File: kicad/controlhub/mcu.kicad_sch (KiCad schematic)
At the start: 0 parts

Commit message: added driver
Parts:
- added U2: ESP32-S3-DevKitC-1-N32R16V, DevKits:ESP32S3DevKitC1N32R16V, symbol DevKits:ESP32-S3-DevKitC-1-N32R16V
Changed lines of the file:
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@@
 	(generator_version "9.0")
 	(paper "A4")
+	(symbol
+		(lib_id "DevKits:ESP32-S3-DevKitC-1-N32R16V")
+		(at 127 38.1 0)
+		(unit 1)
+		(exclude_from_sim no)
+		(in_bom yes)
+		(on_board yes)
+		(dnp no)
+		(fields_autoplaced yes)
+		(property "Reference" "U2"
+			(at 140.97 30.48 0)
+			(effects
+				(font
+					(size 1.27 1.27)
+				)
+			)
+		)
+		(property "Value" "ESP32-S3-DevKitC-1-N32R16V"
+			(at 140.97 33.02 0)
+			(effects
+				(font
+					(size 1.27 1.27)
+				)
+			)
+		)
+		(property "Footprint" "DevKits:ESP32S3DevKitC1N32R16V"
+			(at 151.13 133.02 0)
+			(effects
+				(font
+					(size 1.27 1.27)
+				)
+				(justify left top)
+				(hide yes)
+			)
+		)
+		(property "Datasheet" "https://docs.espressif.com/projects/esp-dev-kits/en/latest/esp32s3/esp-dev-kits-en-master-esp32s3.pdf"
+			(at 151.13 233.02 0)
+			(effects
+				(font
+					(size 1.27 1.27)
+				)
+				(justify left top)
+				(hide yes)
+			)
+		)
+		(property "Description" "Multiprotocol Development Tools The ESP32-S3-DevKitC-1 is an entry-level development board equipped with ESP32-S3-WROOM-1, ESP32-S3-WROOM-1U, or ESP32-S3-WROOM-2, a general-purpose Wi-Fi + Bluetooth Low Energy MCU module that integrates complete Wi-Fi and Bluetooth Low Energy funct"
+			(at 127 38.1 0)
+			(effects
+				(font
+					(size 1.27 1.27)
+				)
+				(hide yes)
+			)
+		)
+		(property "Height" "5"
+			(at 151.13 433.02 0)
+			(effects
+				(font
+					(size 1.27 1.27)
+				)
+				(justify left top)
+				(hide yes)
+			)
+		)
+		(property "Manufacturer_Name" "Espressif Systems"
+			(at 151.13 533.02 0)
+			(effects
+				(font
+					(size 1.27 1.27)
+				)
+				(justify left top)
+				(hide yes)
+			)
+		)
+		(property "Manufacturer_Part_Number" "ESP32-S3-DevKitC-1-N32R16V"
+			(at 151.13 633.02 0)
+			(effects
+				(font
+					(size 1.27 1.27)
+				)
+				(justify left top)
+				(hide yes)
+			)
+		)
+		(property "Mouser Part Number" "356-32S3DKTC1N32R16V"
+			(at 151.13 733.02 0)
+			(effects
+				(font
+					(size 1.27 1.27)
+				)
+				(justify left top)
+				(hide yes)
+			)
+		)
+		(property "Mouser Price/Stock" "https://www.mouser.co.uk/ProductDetail/Espressif-Systems/ESP32-S3-DevKitC-1-N32R16V?qs=sqEgtWRSLJ3pTWIVKUeIew%3D%3D"
+			(at 151.13 833.02 0)
+			(effects
+				(font
+					(size 1.27 1.27)
+				)
+				(justify left top)
+				(hide yes)
+			)
+		)
+		(property "Arrow Part Number" ""
+			(at 151.13 933.02 0)
+			(effects
+				(font
+					(size 1.27 1.27)
+				)
+				(justify left top)
+				(hide yes)
+			)
+		)
+		(property "Arrow Price/Stock" ""
+			(at 151.13 1033.02 0)
+			(effects
+				(font
+					(size 1.27 1.27)
+				)
+				(justify left top)
+				(hide yes)
+			)
+		)
+		(pin "J332"
+		)
+		(pin "J112"
+		)
+		(pin "J116"
+		)
+		(pin "J111"
+		)
+		(pin "J113"
+		)
+		(pin "J114"
+		)
+		(pin "J115"
+		)
+		(pin "J120"
+		)
+		(pin "J317"
+		)
+		(pin "J124"
+		)
+		(pin "J320"
+		)
+		(pin "J322"
+		)
+		(pin "J324"
+		)
+		(pin "J131"
+		)
+		(pin "J130"
+		)
+		(pin "J312"
+		)
+		(pin "J121"
+		)
+		(pin "J118"
+		)
+		(pin "J127"
+		)
+		(pin "J123"
+		)
+		(pin "J128"
+		)
+		(pin "J132"
+		)
+		(pin "J313"
+		)
+		(pin "J117"
+		)
+		(pin "J126"
+		)
+		(pin "J315"
+		)
+		(pin "J122"
+		)
+		(pin "J125"
+		)
+		(pin "J311"
+		)
+		(pin "J314"
+		)
+		(pin "J129"
+		)
+		(pin "J119"
+		)
+		(pin "J316"
+		)
+		(pin "J318"
+		)
+		(pin "J319"
+		)
+		(pin "J321"
+		)
+		(pin "J323"
+		)
+		(pin "J325"
+		)
+		(pin "J331"
+		)
+		(pin "J328"
+		)
+		(pin "J326"
+		)
+		(pin "J329"
+		)
+		(pin "J330"
+		)
+		(pin "J327"
+		)
+		(instances
+			(project ""
+				(path "/78f9b8b9-94ed-46bb-ab2b-797c156bf665/64921508-3e9f-434f-afb3-8d277d43284b"
+					(reference "U2")
+					(unit 1)
+				)
+			)
+		)
+	)
 )

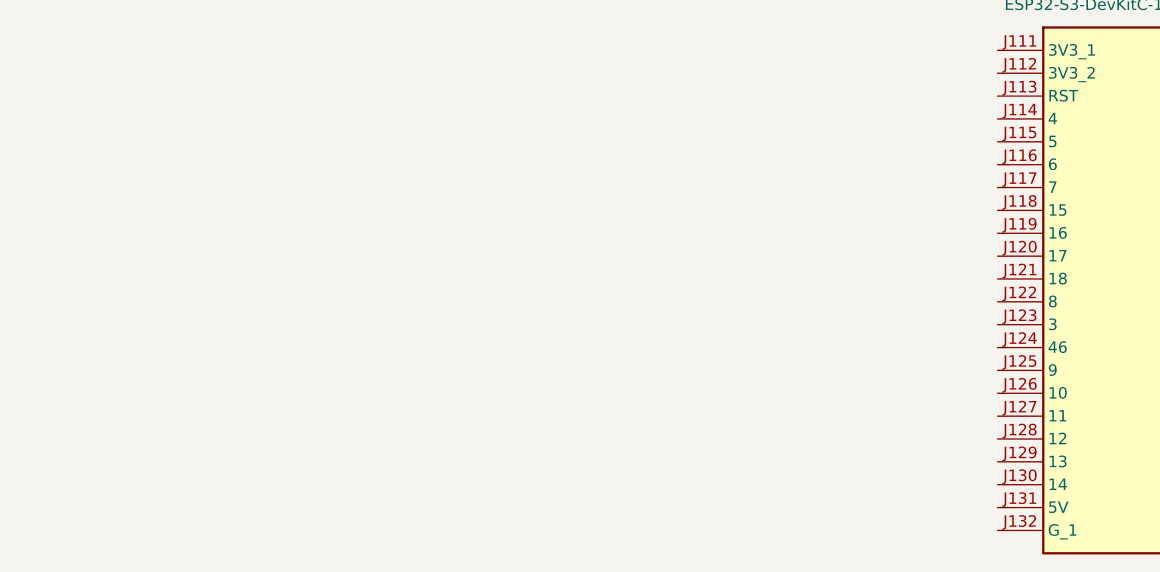
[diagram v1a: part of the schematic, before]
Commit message: removed uneccesary schematics and worked on proper wiring
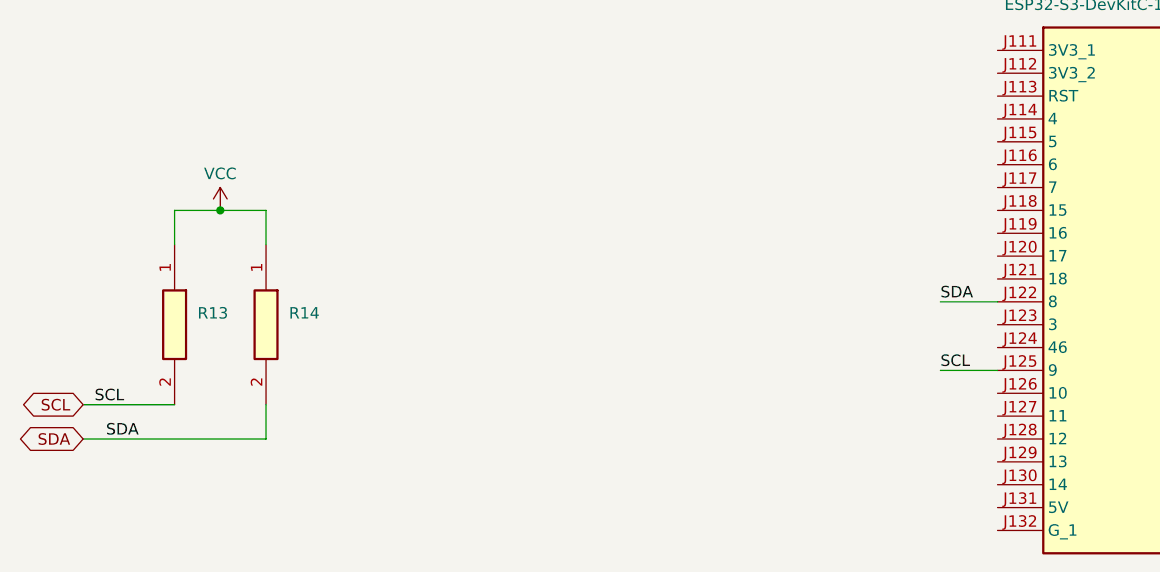
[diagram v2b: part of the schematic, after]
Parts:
- added R13, R14: RC0603JR-072K2L, Resistors:RESC1608X55N, symbol Resistors:RC0603JR-072K2L
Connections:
- net SDA: now reaches U2.J122 (8)
- net SDA: now also R14.2
- net SCL: now reaches U2.J125 (9)
- net SCL: now also R13.2
- new net VCC: R13.1, R14.1

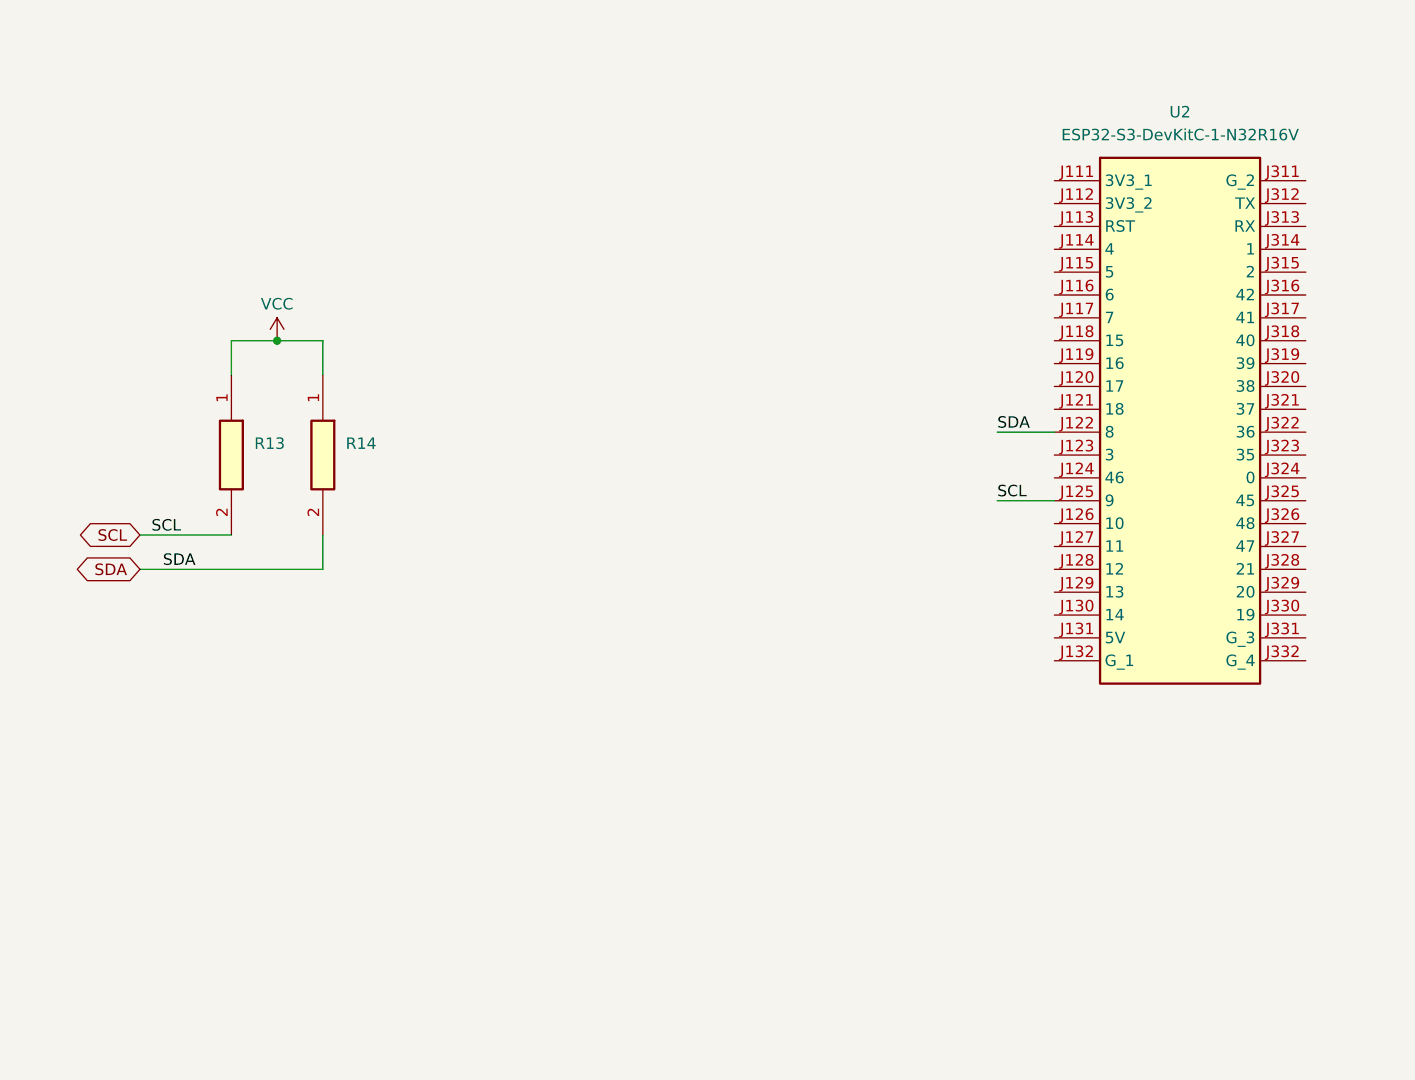
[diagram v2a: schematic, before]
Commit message: added filters and kept working on wiring schematics
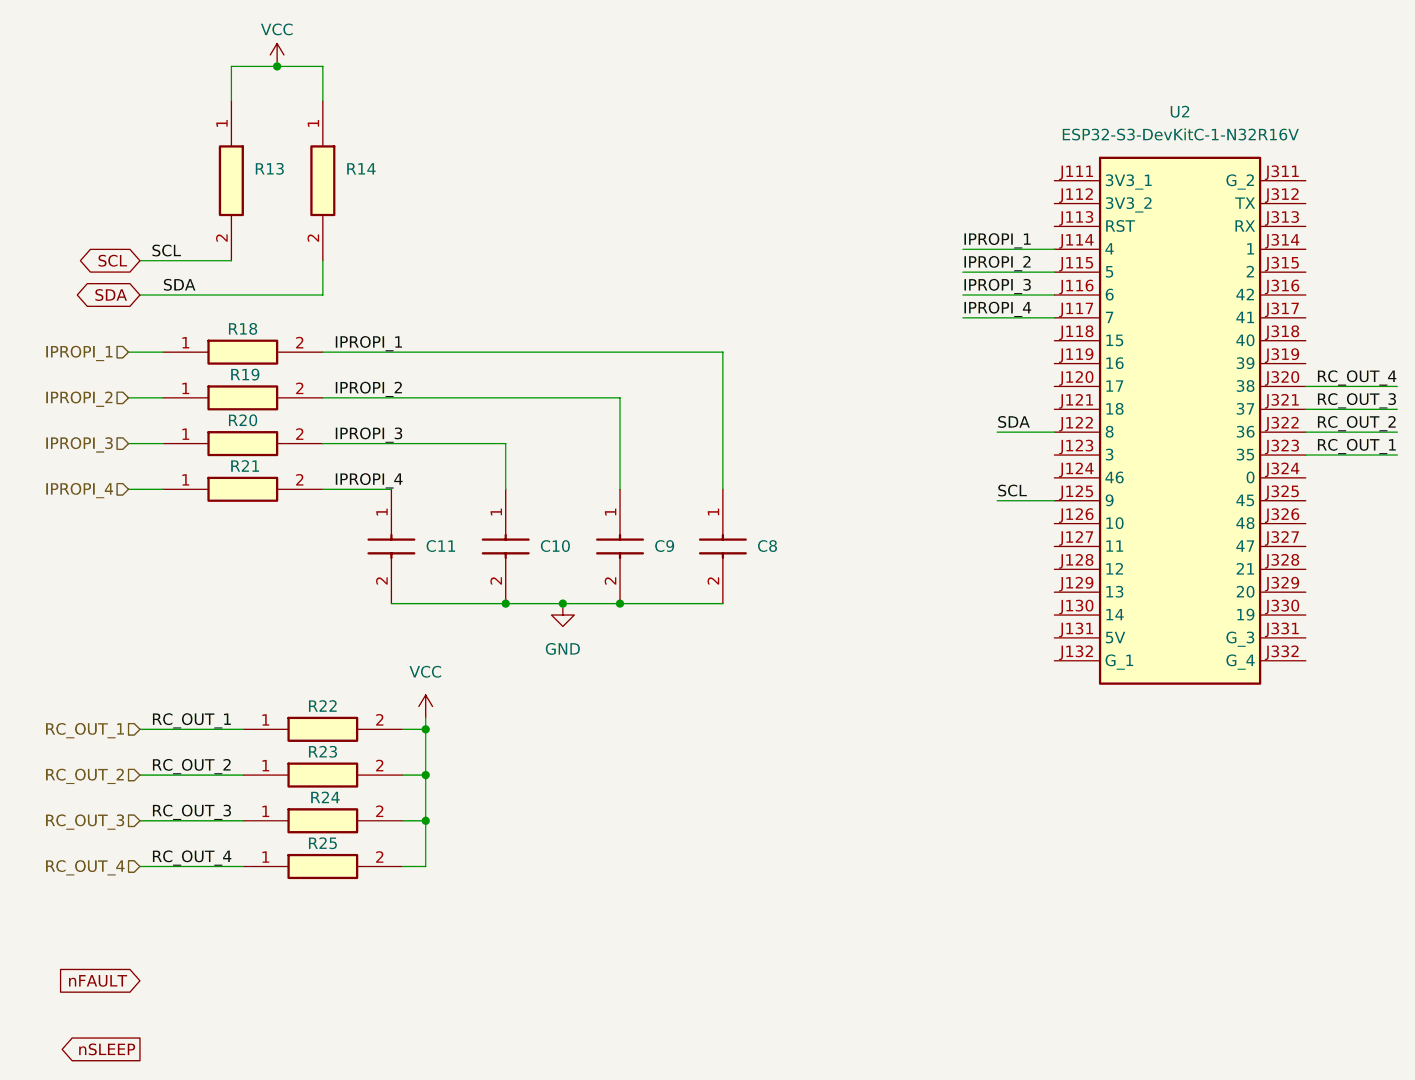
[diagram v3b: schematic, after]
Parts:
- added C10, C11, C9: CGA3E2X7R1H104K080AA, Capacitors:CAPC1608X90N, symbol Capacitors:CGA3E2X7R1H104K080AA
- added C8: CC0603KRX7R9BB472, Capacitors:CAPC1608X90N, symbol Capacitors:CC0603KRX7R9BB472
- added R18, R19, R20, R21: RC0402FR-07100RL, Resistors:RESC1005X40N, symbol Resistors:RC0402FR-07100RL
- added R22, R23, R24, R25: RC0603FR-0710KL, Resistors:RESC1608X55N, symbol Resistors:RC0603FR-0710KL
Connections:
- net VCC: now also R22.2, R23.2, R24.2, R25.2
- net IPROPI_1: now reaches U2.J114 (4)
- net IPROPI_1: now also C8.1, R18.1, R18.2
- net IPROPI_2: now reaches U2.J115 (5)
- net IPROPI_2: now also C9.1, R19.1, R19.2
- net IPROPI_3: now reaches U2.J116 (6)
- net IPROPI_3: now also C10.1, R20.1, R20.2
- net IPROPI_4: now reaches U2.J117 (7)
- net IPROPI_4: now also C11.1, R21.1, R21.2
- net RC_OUT_4: now reaches U2.J320 (38)
- net RC_OUT_4: now also R25.1
- net RC_OUT_3: now reaches U2.J321 (37)
- net RC_OUT_3: now also R24.1
- net RC_OUT_2: now reaches U2.J322 (36)
- net RC_OUT_2: now also R23.1
- net RC_OUT_1: now reaches U2.J323 (35)
- net RC_OUT_1: now also R22.1
- new net GND: C10.2, C11.2, C8.2, C9.2
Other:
- moved on the sheet: R13, R14

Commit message: added more wires in mcu
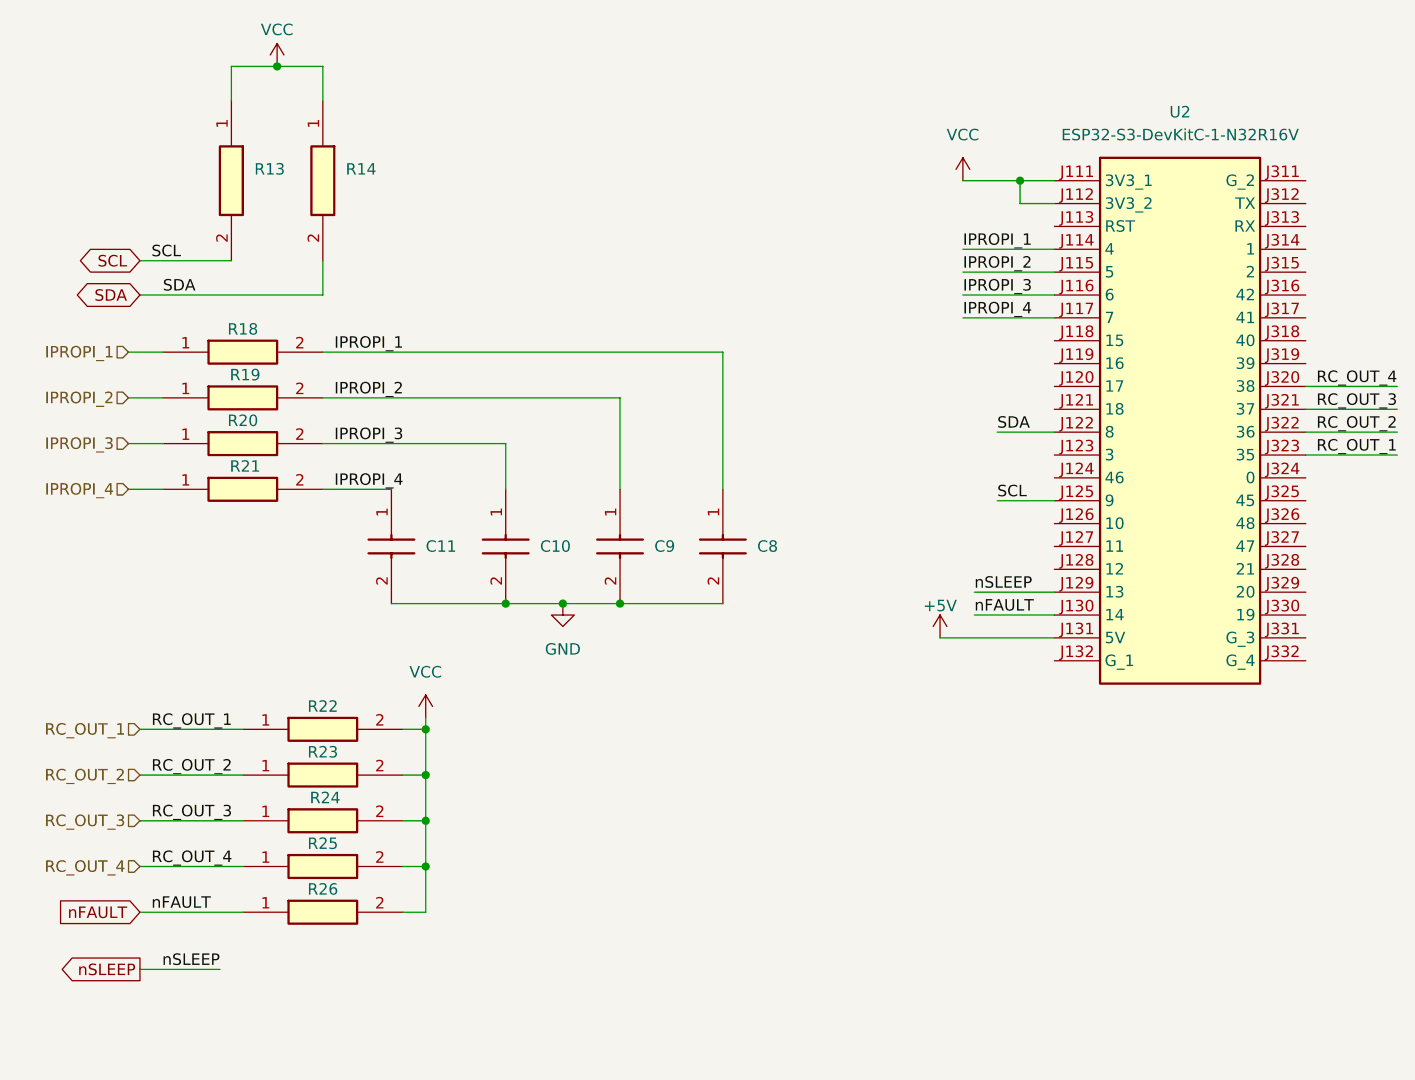
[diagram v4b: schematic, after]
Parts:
- added R26: RC0603FR-0710KL, Resistors:RESC1608X55N, symbol Resistors:RC0603FR-0710KL
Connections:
- net VCC: now also U2.J111 (3V3_1), U2.J112 (3V3_2), R26.2
- net nFAULT: now also U2.J130 (14), R26.1
- net nSLEEP: now also U2.J129 (13)
- net +5V: now reaches U2.J131 (5V)
